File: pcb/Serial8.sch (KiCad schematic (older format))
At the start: 41 parts, among them J1 USB_B, J2 Mini-DIN-8, U1 AM26LV31, U2 CP2102N-A01-GQFN28, U3 AM26LV32

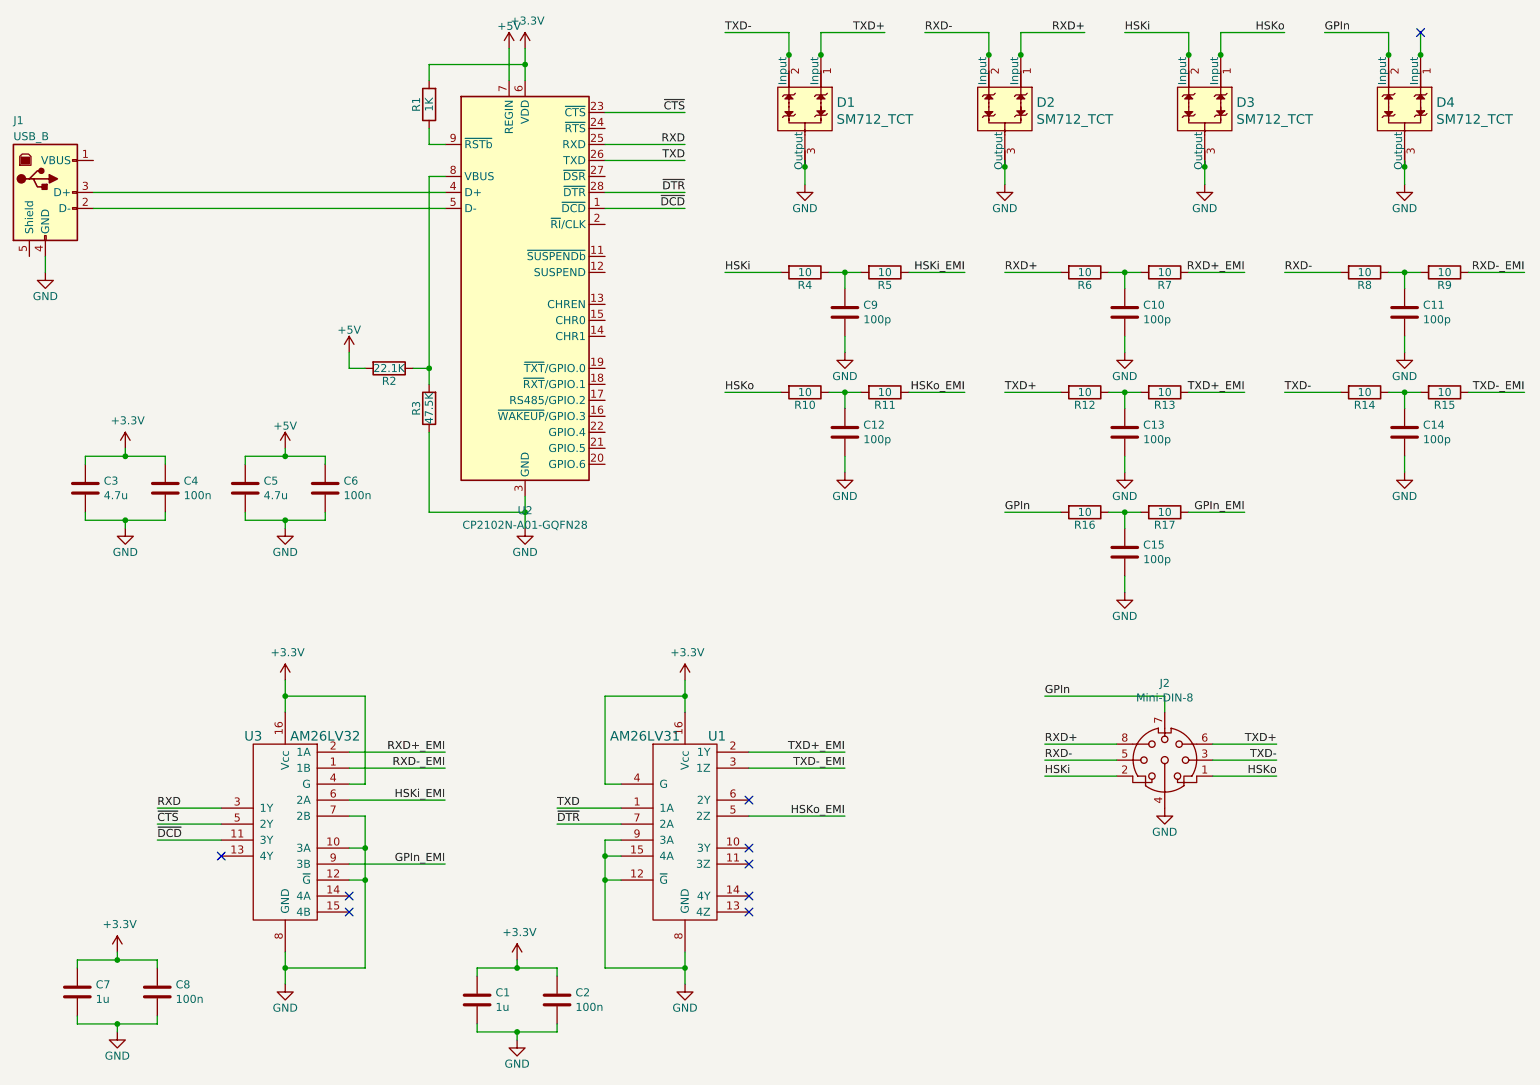
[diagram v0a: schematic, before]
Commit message: Almost finished layout... but probably need some massive change to make it small enough
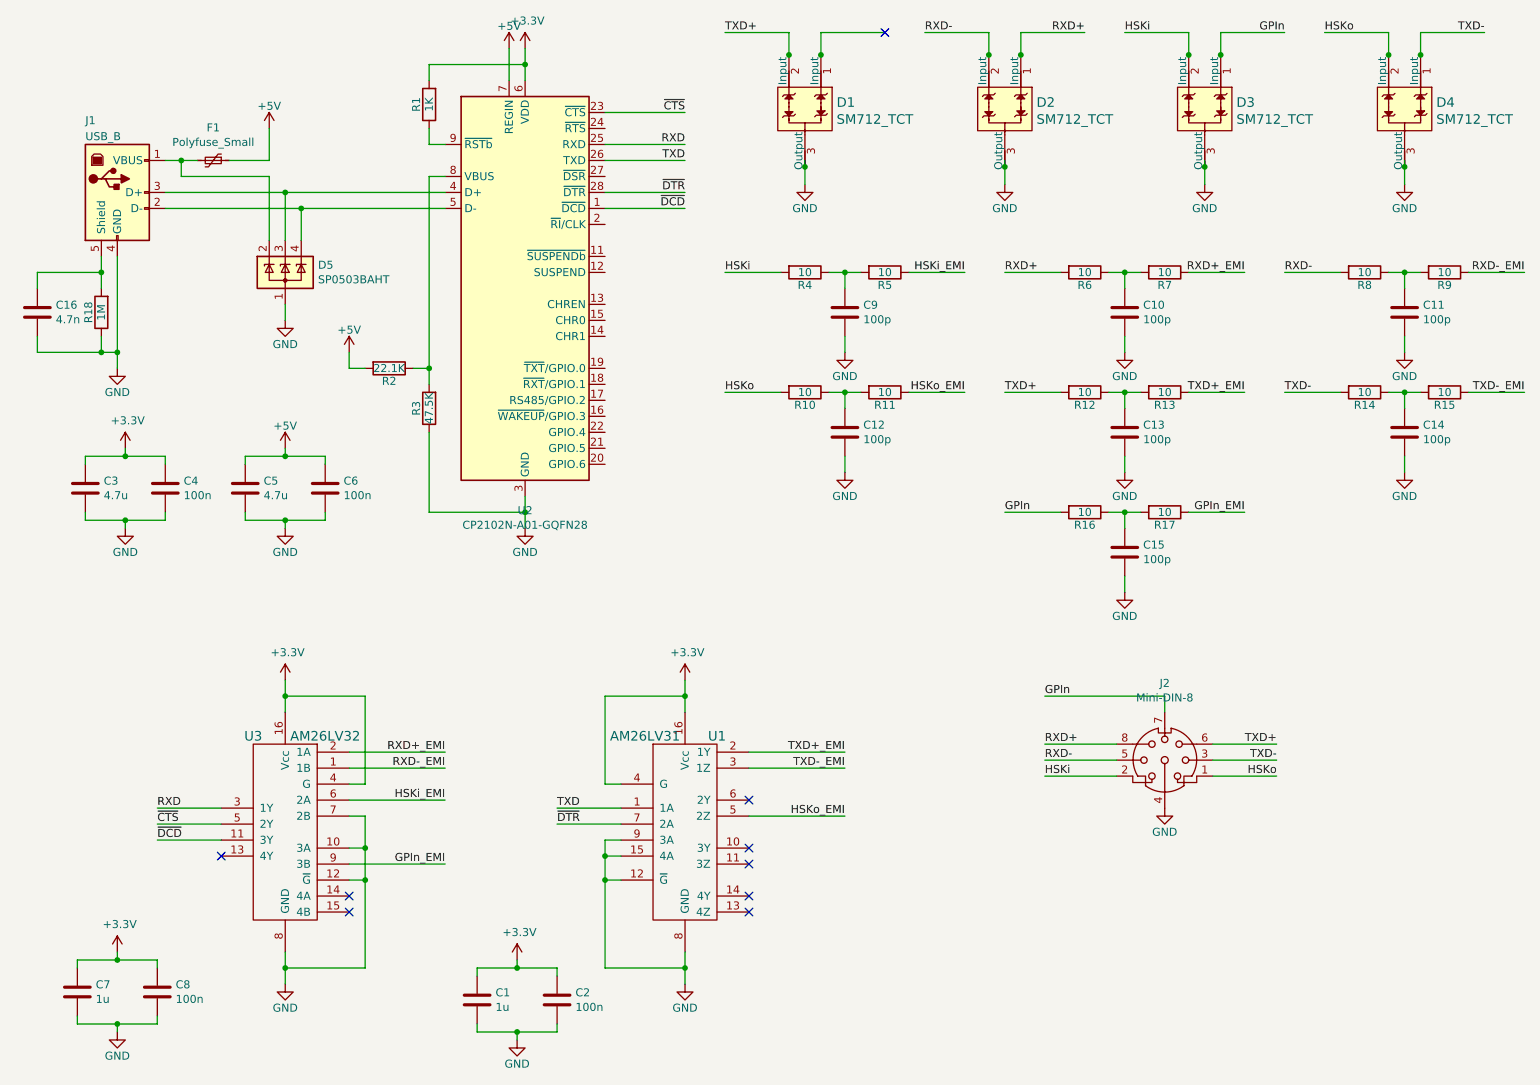
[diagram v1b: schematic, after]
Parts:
- added C16: 4.7n, Capacitors_SMD:C_0603, symbol Device:C
- added D5: SP0503BAHT, Package_TO_SOT_SMD:SOT-143, symbol Power_Protection:SP0503BAHT
- added F1: Polyfuse_Small, Fuse:Fuse_1206_3216Metric, symbol Device:Polyfuse_Small
- added R18: 1M, Resistors_SMD:R_0603, symbol Device:R
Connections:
- wire segments 186 -> 208
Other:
- moved on the sheet: J1
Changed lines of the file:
@@
 L conn:USB_B J1
 U 1 1 5B9743DD
-P 1000 2000
-F 0 "J1" H 800 2450 50  0000 L CNN
-F 1 "USB_B" H 800 2350 50  0000 L CNN
-F 2 "Connect:USB_B" H 1150 1950 50  0001 C CNN
-F 3 "" H 1150 1950 50  0001 C CNN
-	1    1000 2000
-	1    0    0    -1
-$EndComp
-Wire Wire Line
-	3500 2000 1300 2000
-Wire Wire Line
-	1300 2100 3500 2100
+P 1450 2000
+F 0 "J1" H 1250 2450 50  0000 L CNN
+F 1 "USB_B" H 1250 2350 50  0000 L CNN
+F 2 "Connect:USB_B" H 1600 1950 50  0001 C CNN
+F 3 "" H 1600 1950 50  0001 C CNN
+	1    1450 2000
+	1    0    0    -1
+$EndComp
+Wire Wire Line
+	3500 2000 2500 2000
+Wire Wire Line
+	1750 2100 2600 2100
 $Comp
 L Device:R R2
@@
 L power:GND #PWR06
 U 1 1 5B974615
-P 1000 2500
-F 0 "#PWR06" H 1000 2250 50  0001 C CNN
-F 1 "GND" H 1000 2350 50  0000 C CNN
-F 2 "" H 1000 2500 50  0001 C CNN
-F 3 "" H 1000 2500 50  0001 C CNN
-	1    1000 2500
-	1    0    0    -1
-$EndComp
-Wire Wire Line
-	1000 2500 1000 2400
+P 1450 3100
+F 0 "#PWR06" H 1450 2850 50  0001 C CNN
+F 1 "GND" H 1450 2950 50  0000 C CNN
+F 2 "" H 1450 3100 50  0001 C CNN
+F 3 "" H 1450 3100 50  0001 C CNN
+	1    1450 3100
+	1    0    0    -1
+$EndComp
+Wire Wire Line
+	1450 3100 1450 3000
 $Comp
 L rs423:26LS31 U1
@@
 	0    1    1    0
 $EndComp
-Text Label 6250 1000 2    50   ~ 0
+Text Label 5250 1000 0    50   ~ 0
 TXD+
-Text Label 5250 1000 0    50   ~ 0
+Text Label 10000 1000 2    50   ~ 0
 TXD-
 Wire Wire Line
@@
 	0    1    1    0
 $EndComp
-Text Label 8750 1000 2    50   ~ 0
+Text Label 9000 1000 0    50   ~ 0
 HSKo
 Text Label 7750 1000 0    50   ~ 0
@@
 	0    1    1    0
 $EndComp
-Text Label 9000 1000 0    50   ~ 0
+Text Label 8750 1000 2    50   ~ 0
 GPIn
 Wire Wire Line
@@
 Wire Wire Line
 	9500 1840 9500 1950
-NoConn ~ 9600 1000
 $Comp
 L Device:C C7
@@
 Wire Wire Line
 	6750 3250 6400 3250
+$Comp
+L Power_Protection:SP0503BAHT D5
+U 1 1 5EEE31B6
+P 2500 2500
+F 0 "D5" H 2705 2546 50  0000 L CNN
+F 1 "SP0503BAHT" H 2705 2455 50  0000 L CNN
+F 2 "Package_TO_SOT_SMD:SOT-143" H 2725 2450 50  0001 L CNN
+F 3 "http://www.littelfuse.com/~/media/files/littelfuse/technical%20resources/documents/data%20sheets/sp05xxba.pdf" H 2625 2625 50  0001 C CNN
+	1    2500 2500
+	1    0    0    -1
+$EndComp
+$Comp
+L power:GND #PWR0101
+U 1 1 5EEE418D
+P 2500 2800
+F 0 "#PWR0101" H 2500 2550 50  0001 C CNN
+F 1 "GND" H 2500 2650 50  0000 C CNN
+F 2 "" H 2500 2800 50  0001 C CNN
+F 3 "" H 2500 2800 50  0001 C CNN
+	1    2500 2800
+	1    0    0    -1
+$EndComp
+Wire Wire Line
+	2500 2800 2500 2700
+Wire Wire Line
+	2400 1800 2150 1800
+Wire Wire Line
+	2500 2300 2500 2000
+Connection ~ 2500 2000
+Wire Wire Line
+	2500 2000 1750 2000
+Wire Wire Line
+	2600 2300 2600 2100
+Connection ~ 2600 2100
+Wire Wire Line
+	2600 2100 3500 2100
+$Comp
+L Device:R R18
+U 1 1 5EF1103E
+P 1350 2750
+F 0 "R18" V 1430 2750 50  0000 C CNN
+F 1 "1M" V 1350 2750 50  0000 C CNN
+F 2 "Resistors_SMD:R_0603" V 1280 2750 50  0001 C CNN
+F 3 "" H 1350 2750 50  0001 C CNN
+	1    1350 2750
+	-1   0    0    1
+$EndComp
+$Comp
+L Device:C C16
+U 1 1 5EF11508
+P 950 2750
+F 0 "C16" H 1065 2796 50  0000 L CNN
+F 1 "4.7n" H 1065 2705 50  0000 L CNN
+F 2 "Capacitors_SMD:C_0603" H 988 2600 50  0001 C CNN
+F 3 "~" H 950 2750 50  0001 C CNN
+	1    950  2750
+	1    0    0    -1
+$EndComp
+Wire Wire Line
+	1450 3000 1350 3000
+Wire Wire Line
+	950  3000 950  2900
+Connection ~ 1450 3000
+Wire Wire Line
+	1450 3000 1450 2400
+Wire Wire Line
+	1350 2900 1350 3000
+Connection ~ 1350 3000
+Wire Wire Line
+	1350 3000 950  3000
+Wire Wire Line
+	1350 2400 1350 2500
+Wire Wire Line
+	1350 2500 950  2500
+Wire Wire Line
+	950  2500 950  2600
+Connection ~ 1350 2500
+Wire Wire Line
+	1350 2500 1350 2600
+$Comp
+L Device:Polyfuse_Small F1
+U 1 1 5EF6C892
+P 2050 1800
+F 0 "F1" V 1845 1800 50  0000 C CNN
+F 1 "Polyfuse_Small" V 1936 1800 50  0000 C CNN
+F 2 "Fuse:Fuse_1206_3216Metric" H 2100 1600 50  0001 L CNN
+F 3 "~" H 2050 1800 50  0001 C CNN
+	1    2050 1800
+	0    1    1    0
+$EndComp
+Wire Wire Line
+	1950 1800 1850 1800
+$Comp
+L power:+5V #PWR0102
+U 1 1 5EF964DB
+P 2400 1600
+F 0 "#PWR0102" H 2400 1450 50  0001 C CNN
+F 1 "+5V" H 2400 1740 50  0000 C CNN
+F 2 "" H 2400 1600 50  0001 C CNN
+F 3 "" H 2400 1600 50  0001 C CNN
+	1    2400 1600
+	1    0    0    -1
+$EndComp
+Wire Wire Line
+	2400 1800 2400 1600
+Wire Wire Line
+	1850 1800 1850 1900
+Wire Wire Line
+	1850 1900 2400 1900
+Wire Wire Line
+	2400 1900 2400 2300
+Connection ~ 1850 1800
+Wire Wire Line
+	1850 1800 1750 1800
+Wire Wire Line
+	10000 1000 9600 1000
+NoConn ~ 6250 1000
 $EndSCHEMATC
